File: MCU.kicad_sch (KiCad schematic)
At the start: 95 parts, among them J501 HX JN1.27-2x5P ZZ H4.9, J502 Header, U501 STM32G431K8Tx, Y501 20 MHz

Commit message: updating BOM info
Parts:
- C501, C505, C506, D501, D502, J502, R501, R503, R504, R505, R506, R507: Manufacturer (none) -> Generic
- C502, C503, C504: Manufacturer (none) -> CCTC; Manufacturer Part Number (none) -> TCC0603X7R104K500CT
- J501: Field5 https://www.lcsc.com/product-detail/IDC-Connectors_hanxia-H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 -> (none); Manufacturer (none) -> hanxia; Manufacturer Part Number (none) -> HX JN1.27-2x5P ZZ H4.9
- TP501, TP502, TP503, TP504, TP505, TP506, TP507, TP508, TP509, TP510, TP511, TP512, TP513, TP514, TP515, TP516, TP517: now left out of the parts list
- U501: Manufacturer (none) -> STMicroelectronics; Manufacturer Part Number (none) -> STM32G431K8T6
- Y501: Manufacturer (none) -> huaxindianzi; Manufacturer Part Number (none) -> CF4020M00018001

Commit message: Sch update in progress
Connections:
- net I_P_buf renamed Mon_IL_prot
- net I_SH1000 renamed I_S1k
- net Lamp_EN renamed LMP_EN
- net U_C_buf renamed Mon_LMP_buf
- net U_L_buf renamed Mon_S1k_buf
- net U_SH1000_buf renamed U_S1k_buf
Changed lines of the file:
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@@
 		)
 	)
-	(label "I_SH1000"
+	(label "I_S1k"
 		(at 184.15 95.25 180)
 		(effects
@@
 		)
 	)
-	(label "I_P_buf"
+	(label "Mon_IL_prot"
 		(at 184.15 100.33 180)
 		(effects
@@
 		)
 	)
-	(label "Lamp_EN"
+	(label "LMP_EN"
 		(at 110.49 26.67 180)
 		(effects
@@
 		)
 	)
-	(label "I_SH1000"
+	(label "I_S1k"
 		(at 50.8 55.88 180)
 		(effects
@@
 		)
 	)
-	(label "U_SH1000_buf"
+	(label "U_S1k_buf"
 		(at 184.15 87.63 180)
 		(effects
@@
 		)
 	)
-	(label "U_C_buf"
+	(label "Mon_LMP_buf"
 		(at 184.15 102.87 180)
 		(effects
@@
 		)
 	)
-	(label "U_L_buf"
+	(label "Mon_S1k_buf"
 		(at 184.15 97.79 180)
 		(effects
@@
 		)
 	)
-	(label "U_L_buf"
+	(label "Mon_S1k_buf"
 		(at 50.8 40.64 180)
 		(effects
@@
 		)
 	)
-	(label "Lamp_EN"
+	(label "LMP_EN"
 		(at 50.8 60.96 180)
 		(effects
@@
 		)
 	)
-	(label "I_P_buf"
+	(label "Mon_IL_prot"
 		(at 50.8 45.72 180)
 		(effects
@@
 		)
 	)
-	(label "U_SH1000_buf"
+	(label "U_S1k_buf"
 		(at 50.8 50.8 180)
 		(effects
@@
 		)
 	)
-	(label "U_C_buf"
+	(label "Mon_LMP_buf"
 		(at 50.8 43.18 180)
 		(effects
@@
 		)
 	)
-	(hierarchical_label "Lamp_EN"
+	(hierarchical_label "LMP_EN"
 		(shape output)
 		(at 33.02 60.96 180)
@@
 		)
 	)
-	(hierarchical_label "U_L_buf"
+	(hierarchical_label "Mon_S1k_buf"
 		(shape input)
 		(at 33.02 40.64 180)
@@
 		)
 	)
-	(hierarchical_label "I_SH1000"
+	(hierarchical_label "I_S1k"
 		(shape input)
 		(at 33.02 55.88 180)
@@
 		)
 	)
-	(hierarchical_label "U_C_buf"
+	(hierarchical_label "Mon_LMP_buf"
 		(shape input)
 		(at 33.02 43.18 180)
@@
 		)
 	)
-	(hierarchical_label "I_P_buf"
+	(hierarchical_label "Mon_IL_prot"
 		(shape input)
 		(at 33.02 45.72 180)
@@
 		)
 	)
-	(hierarchical_label "U_SH1000_buf"
+	(hierarchical_label "U_S1k_buf"
 		(shape input)
 		(at 33.02 50.8 180)

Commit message: Sch update in progres
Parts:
- removed J502: Header, Connector_PinHeader_2.54mm:PinHeader_1x02_P2.54mm_Vertical, symbol Connector:Conn_01x02_Pin
- removed P540, P706, P738: ~, symbol personal:Cosmetic_IN
- removed P750, P751, P752, P753, P762: ~, symbol personal:Cosmetic_OUT
- removed P778, P781: ~, symbol personal:Cosmetic_PWR
- removed R506: 0R, Resistor_SMD:R_0603_1608Metric_Pad0.98x0.95mm_HandSolder, symbol Device:R
- added C109: 100n, Capacitor_SMD:C_0603_1608Metric_Pad1.08x0.95mm_HandSolder, symbol Device:C
- added P108, P131, P132, P135, P136: ~, symbol personal:Cosmetic_GND
- added P133: ~, symbol personal:Cosmetic_OUT
- added P134: ~, symbol personal:Cosmetic_IN
- added TP518, TP519, TP520: TestPoint, TestPoint:TestPoint_THTPad_D1.0mm_Drill0.5mm, symbol Connector:TestPoint
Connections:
- net SH3_A is gone; now on net SH3: C504.1, U501.15 (VDDA)
- net BOOT0: now also TP518.1
- net HV_NRST: now also C109.1
- net SH0: now also C109.2, P108.1, P131.1, P132.1, P135.1, P136.1, TP519.1, TP520.1
- net I_S1k renamed SUP_RX
- net SUP_RX: now also P133.1
- net I_SH240 renamed SUP_TX
- net SUP_TX: now also P134.1
- net U_S1k_buf: no longer names the net of TP501.1, U501.5 (PA0)
- net U_SH240_buf: no longer names the net of TP502.1, U501.6 (PA1)
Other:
- note removed: "Boot config"
- moved on the sheet: C501, C502, C503, C504, C505, C506, D501, D502, R503, R504, R505, R507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

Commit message: Placement 50%
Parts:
- removed J501: HX JN1.27-2x5P ZZ H4.9, Personal:HX JN1.27-2x5P ZZ H4.9, symbol Connector_Generic:Conn_02x05_Odd_Even
- removed P513, P777: ~, symbol personal:Cosmetic_PWR
- removed P522: ~, symbol personal:Cosmetic_IO
- removed P760, P761: ~, symbol personal:Cosmetic_OUT
- removed P773, P774: ~, symbol personal:Cosmetic_GND
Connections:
- no-connect marks 3 -> 0
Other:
- note removed: "SWD header - HV side"

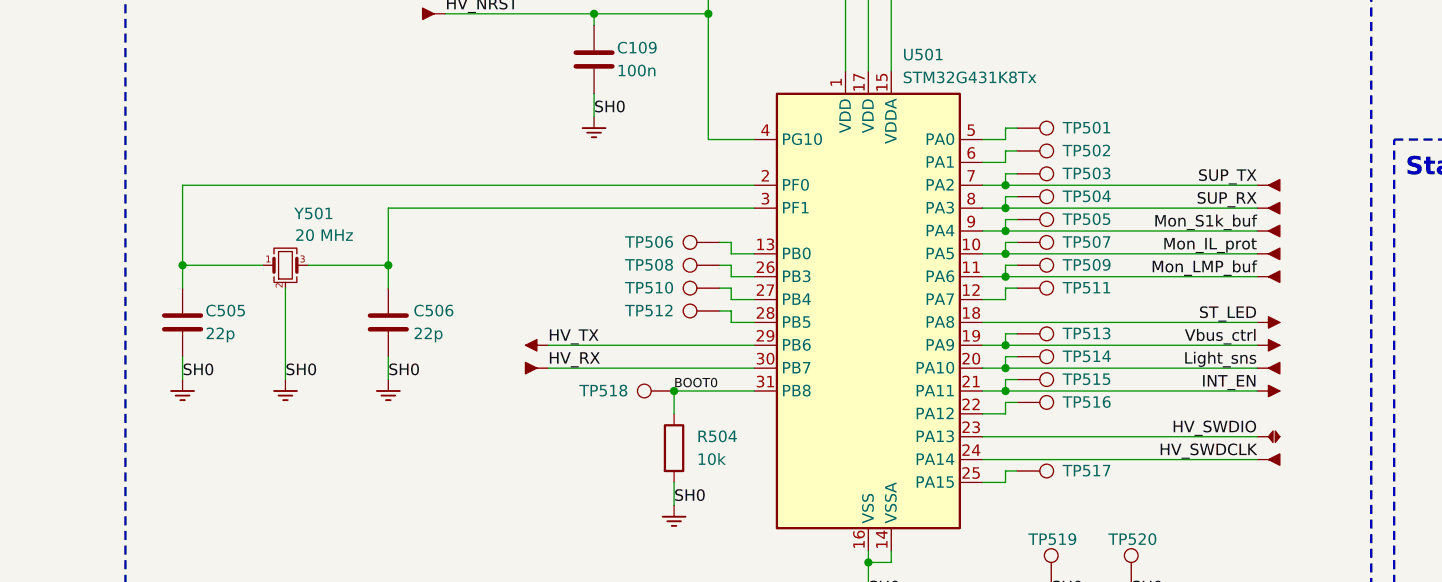
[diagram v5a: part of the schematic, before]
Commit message: Placement complplete, feasibility routing complete
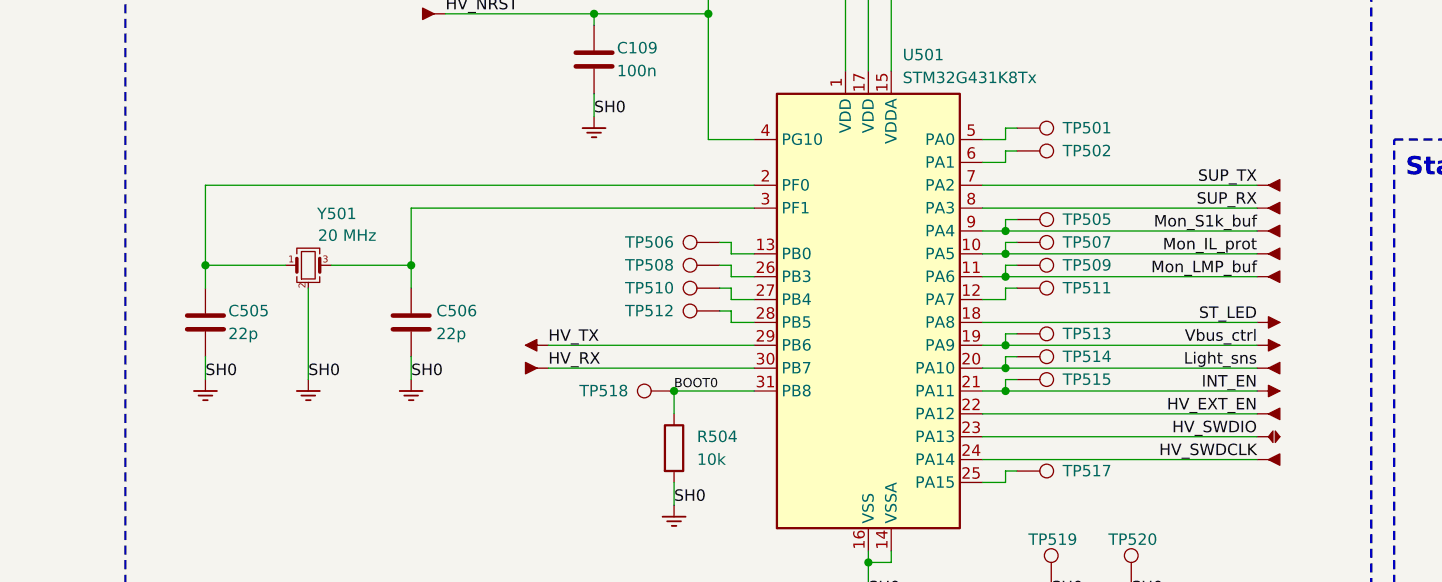
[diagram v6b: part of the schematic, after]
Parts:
- removed TP503, TP504, TP516: TestPoint, TestPoint:TestPoint_THTPad_D1.0mm_Drill0.5mm, symbol Connector:TestPoint
- added P140: ~, symbol personal:Cosmetic_IN
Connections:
- net HV_EXT_EN: now also U501.22 (PA12), P140.1
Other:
- moved on the sheet: C505, C506, Y501

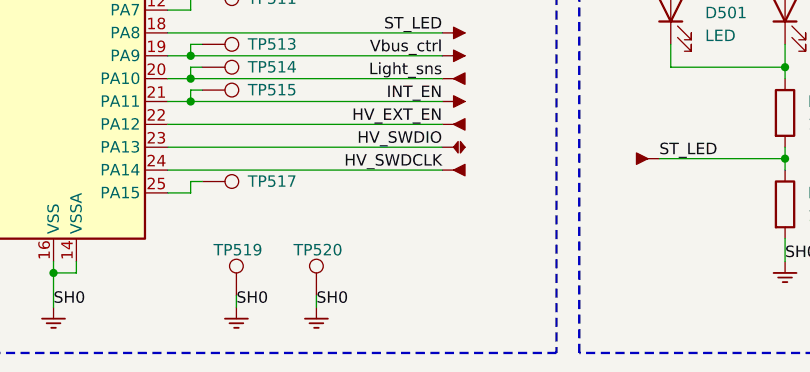
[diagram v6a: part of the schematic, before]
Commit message: Routing complete, silk to do, vias to check, one footprint to update
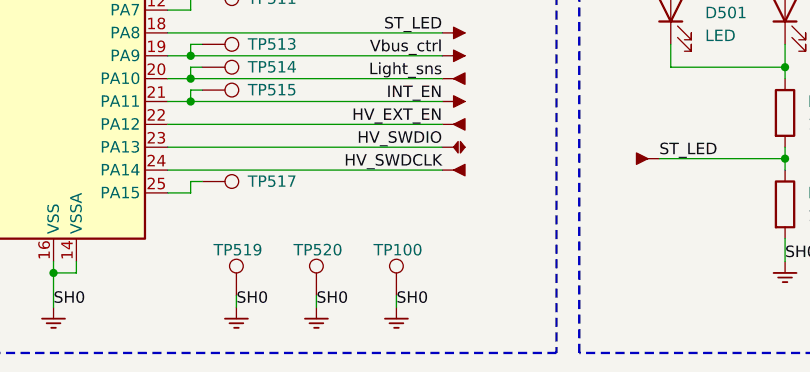
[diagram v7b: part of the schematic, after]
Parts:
- added P141: ~, symbol personal:Cosmetic_GND
- added TP100: TestPoint, TestPoint:TestPoint_THTPad_D1.0mm_Drill0.5mm, symbol Connector:TestPoint
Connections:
- net SH0: now also P141.1, TP100.1
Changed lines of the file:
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@@
 	(wire
 		(pts
+			(xy 179.07 146.05) (xy 179.07 147.32)
+		)
+		(stroke
+			(width 0)
+			(type default)
+		)
+	)
+	(wire
+		(pts
 			(xy 153.67 99.06) (xy 156.21 99.06)
 		)
@@
 		)
 	)
+	(label "SH0"
+		(at 179.07 147.32 0)
+		(effects
+			(font
+				(size 1.27 1.27)
+			)
+			(justify left bottom)
+		)
+	)
 	(label "Mon_LMP_buf"
 		(at 184.15 111.76 180)
@@
 	)
 	(symbol
+		(lib_id "Connector:TestPoint")
+		(at 179.07 146.05 0)
+		(unit 1)
+		(exclude_from_sim no)
+		(in_bom no)
+		(on_board yes)
+		(dnp no)
+		(property "Reference" "TP100"
+			(at 176.53 140.97 0)
+			(effects
+				(font
+					(size 1.27 1.27)
+				)
+				(justify left)
+			)
+		)
+		(property "Value" "TestPoint"
+			(at 180.3399 140.97 90)
+			(effects
+				(font
+					(size 1.27 1.27)
+				)
+				(justify left)
+				(hide yes)
+			)
+		)
+		(property "Footprint" "TestPoint:TestPoint_THTPad_D1.0mm_Drill0.5mm"
+			(at 184.15 146.05 0)
+			(effects
+				(font
+					(size 1.27 1.27)
+				)
+				(hide yes)
+			)
+		)
+		(property "Datasheet" "~"
+			(at 184.15 146.05 0)
+			(effects
+				(font
+					(size 1.27 1.27)
+				)
+				(hide yes)
+			)
+		)
+		(property "Description" "test point"
+			(at 179.07 146.05 0)
+			(effects
+				(font
+					(size 1.27 1.27)
+				)
+				(hide yes)
+			)
+		)
+		(property "Config" ""
+			(at 179.07 146.05 90)
+			(effects
+				(font
+					(size 1.27 1.27)
+				)
+				(hide yes)
+			)
+		)
+		(property "Manufacturer" ""
+			(at 179.07 146.05 90)
+			(effects
+				(font
+					(size 1.27 1.27)
+				)
+				(hide yes)
+			)
+		)
+		(property "Manufacturer Part Number" ""
+			(at 179.07 146.05 90)
+			(effects
+				(font
+					(size 1.27 1.27)
+				)
+				(hide yes)
+			)
+		)
+		(pin "1"
+		)
+		(instances
+			(project "Strobe_main"
+				(path "/f9e05184-c88b-4a88-ae9c-ab2bdb32be7c/82da9dbf-ba38-4d08-ba35-a220fa2963b1/ff259134-84db-47d3-8250-13ef5aa350b1"
+					(reference "TP100")
+					(unit 1)
+				)
+			)
+		)
+	)
+	(symbol
 		(lib_id "personal:Cosmetic_IN")
 		(at 184.15 111.76 180)
@@
 					(unit 1)
 				)
+			)
+		)
+	)
+	(symbol
+		(lib_id "personal:Cosmetic_GND")
+		(at 179.07 147.32 0)
+		(unit 1)
+		(exclude_from_sim no)
+		(in_bom no)
+		(on_board no)
+		(dnp no)
+		(fields_autoplaced yes)
+		(property "Reference" "P141"
+			(at 179.07 146.304 0)
+			(effects
+				(font
+					(size 1.27 1.27)
+				)
+				(hide yes)
+			)
+		)
+		(property "Value" "~"
+			(at 181.61 148.5138 0)
+			(effects
+				(font
+					(size 1.27 1.27)
+				)
+				(justify left)
+				(hide yes)
+			)
+		)
+		(property "Footprint" ""
+			(at 179.07 147.32 0)
+			(effects
+				(font
+					(size 1.27 1.27)
+				)
+				(hide yes)
+			)
+		)
+		(property "Datasheet" ""
+			(at 179.07 147.32 0)
+			(effects
+				(font
+					(size 1.27 1.27)
+				)
+				(hide yes)
+			)
+		)
+		(property "Description" ""
+			(at 179.07 147.32 0)
+			(effects
+				(font
+					(size 1.27 1.27)
+				)
+				(hide yes)
+			)
+		)
+		(property "Config" ""
+			(at 179.07 147.32 0)
+			(effects
+				(font
+					(size 1.27 1.27)
+				)
+				(hide yes)
+			)
+		)
+		(property "Manufacturer" ""
+			(at 179.07 147.32 0)
+			(effects
+				(font
+					(size 1.27 1.27)
+				)
+				(hide yes)
+			)
+		)
+		(property "Manufacturer Part Number" ""
+			(at 179.07 147.32 0)
+			(effects
+				(font
+					(size 1.27 1.27)
+				)
+				(hide yes)
+			)
+		)
+		(pin "1"
+		)
+		(instances
+			(project "Strobe_main"
+				(path "/f9e05184-c88b-4a88-ae9c-ab2bdb32be7c/82da9dbf-ba38-4d08-ba35-a220fa2963b1/ff259134-84db-47d3-8250-13ef5aa350b1"
+					(reference "P141")
+					(unit 1)
+				)

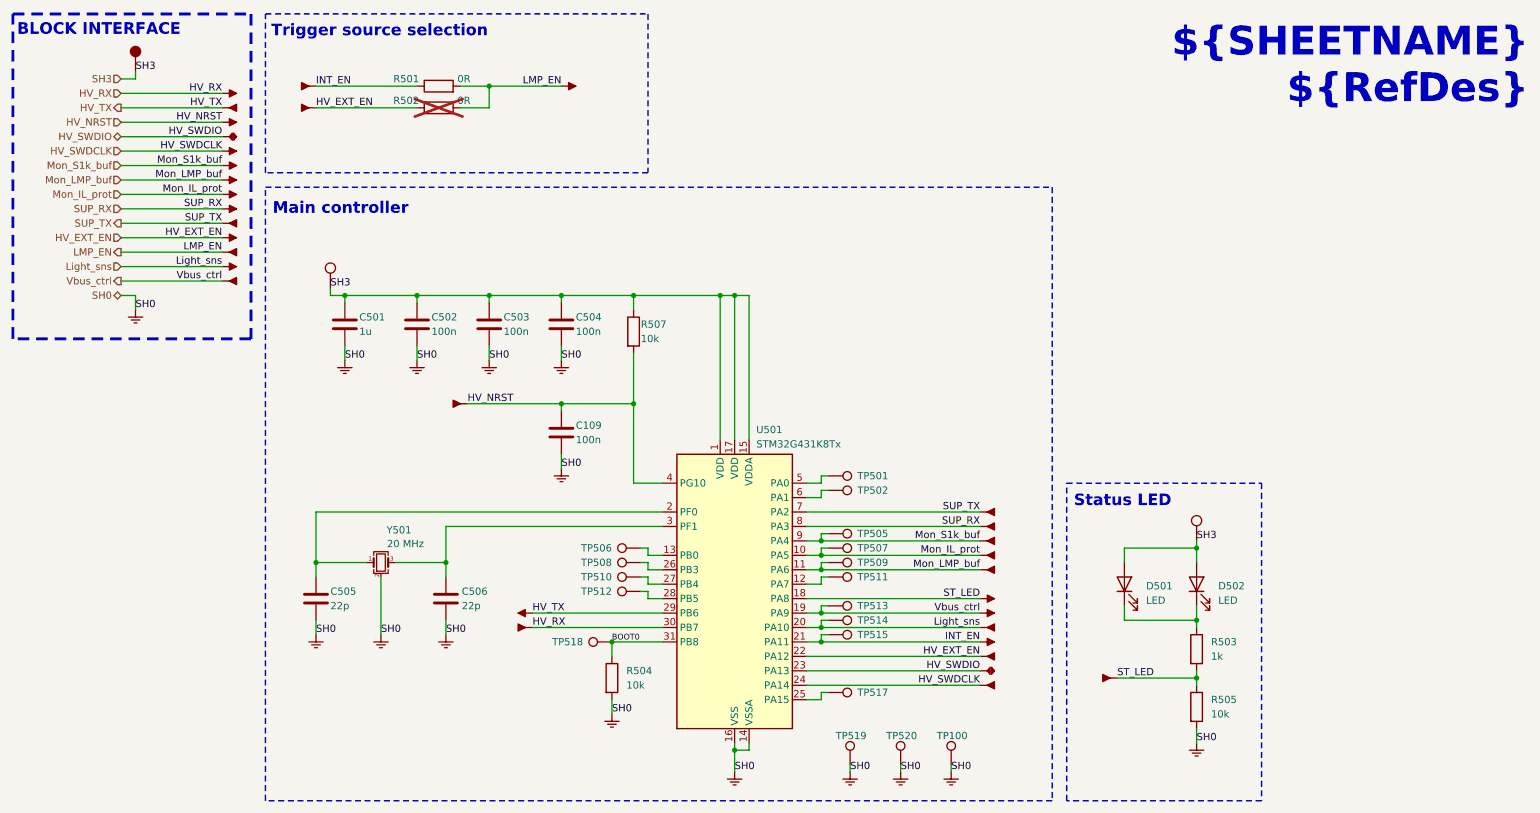
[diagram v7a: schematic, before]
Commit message: Reannotated, silk done, missing some 3D models
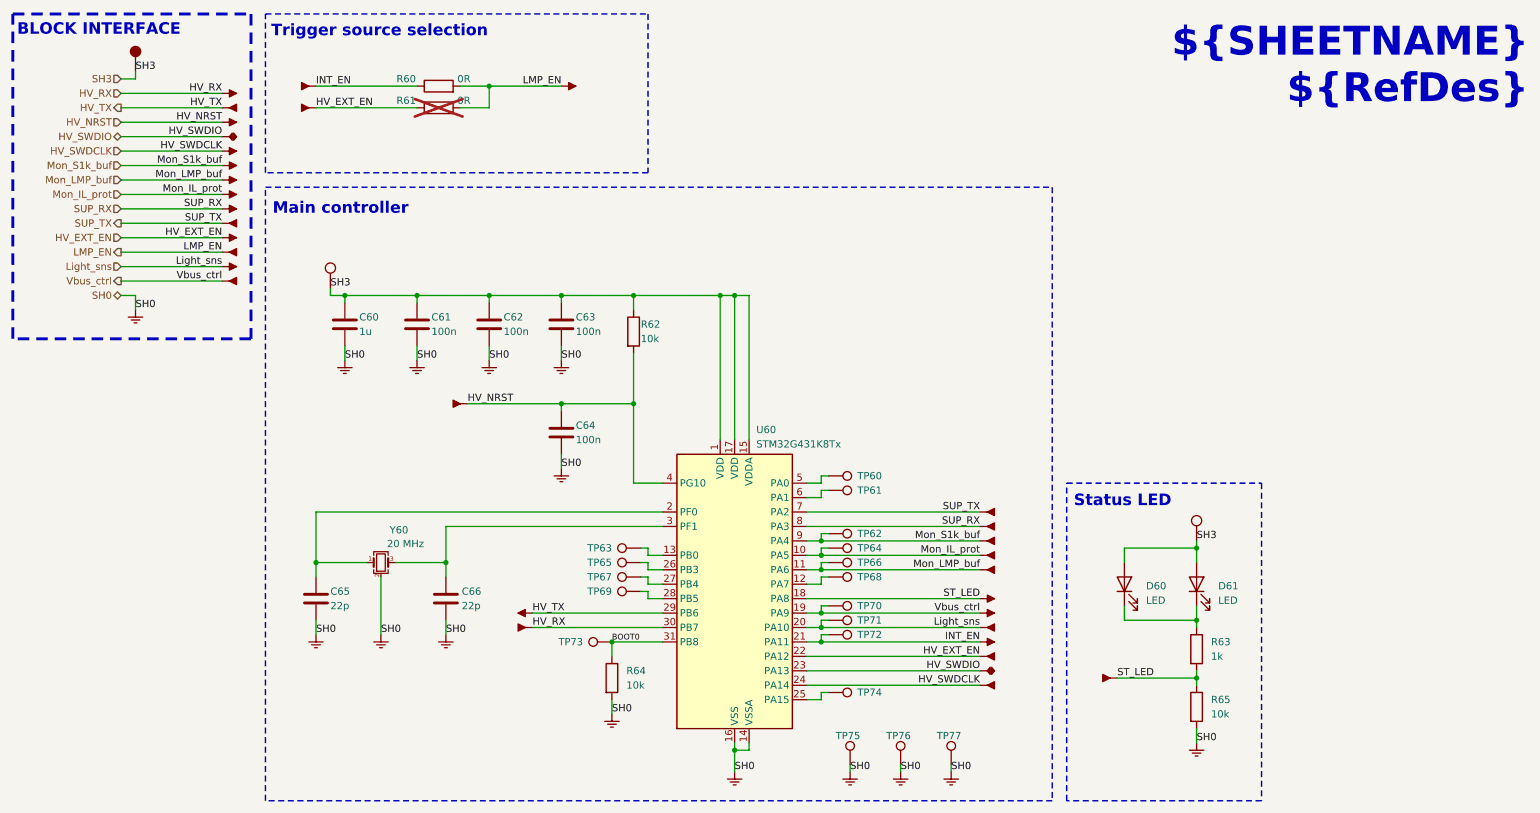
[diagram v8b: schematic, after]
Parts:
- renumbered C501 to C60, C502 to C61, C503 to C62, C504 to C63, C109 to C64, C505 to C65, C506 to C66, D501 to D60, D502 to D61, P501 to P108, P763 to P131, P754 to P132, P747 to P133, P741 to P134, P764 to P135, P745 to P136, P776 to P139, P744 to P140, P746 to P141, P748 to P142, P749 to P143, P133 to P144, P134 to P145, P755 to P146, P742 to P147, P529 to P148, P743 to P149, P780 to P150, P772 to P151, P769 to P152, P108 to P153, P131 to P154, P768 to P155, P739 to P156, P132 to P157, P732 to P158, P733 to P159, P734 to P160, P779 to P161, P735 to P162, P736 to P163, P756 to P164, P759 to P165, P757 to P166, P737 to P167, P708 to P168, P553 to P169, P765 to P170, P766 to P171, P758 to P172, P140 to P173, P775 to P174, P740 to P175, P707 to P176, P770 to P177, P771 to P178, P767 to P179, P135 to P180, P136 to P181, P141 to P182, R501 to R60, R502 to R61, R507 to R62, R503 to R63, R504 to R64, R505 to R65, TP501 to TP60, TP502 to TP61, TP505 to TP62, TP506 to TP63, TP507 to TP64, TP508 to TP65, TP509 to TP66, TP510 to TP67, TP511 to TP68, TP512 to TP69, TP513 to TP70, TP514 to TP71, TP515 to TP72, TP518 to TP73, TP517 to TP74, TP519 to TP75, TP520 to TP76, TP100 to TP77, U501 to U60, Y501 to Y60
